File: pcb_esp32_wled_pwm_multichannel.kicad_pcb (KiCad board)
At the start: 4 copper layers, 164.6 x 48.3 mm, 94 parts, among them J101 WJ2EDGRC-5.08-4P, J102 WJ2EDGRC-5.08-4P, J103 WJ2EDGRC-5.08-4P, J104 WJ2EDGRC-5.08-4P, J105 Conn_01x05_Male, J106 Conn_01x03_Female, J107 Conn_01x03_Female, J108 Conn_01x02_Female, J109 USB_C_Receptacle_USB2.0, Q101 IRLR8743TRPBF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

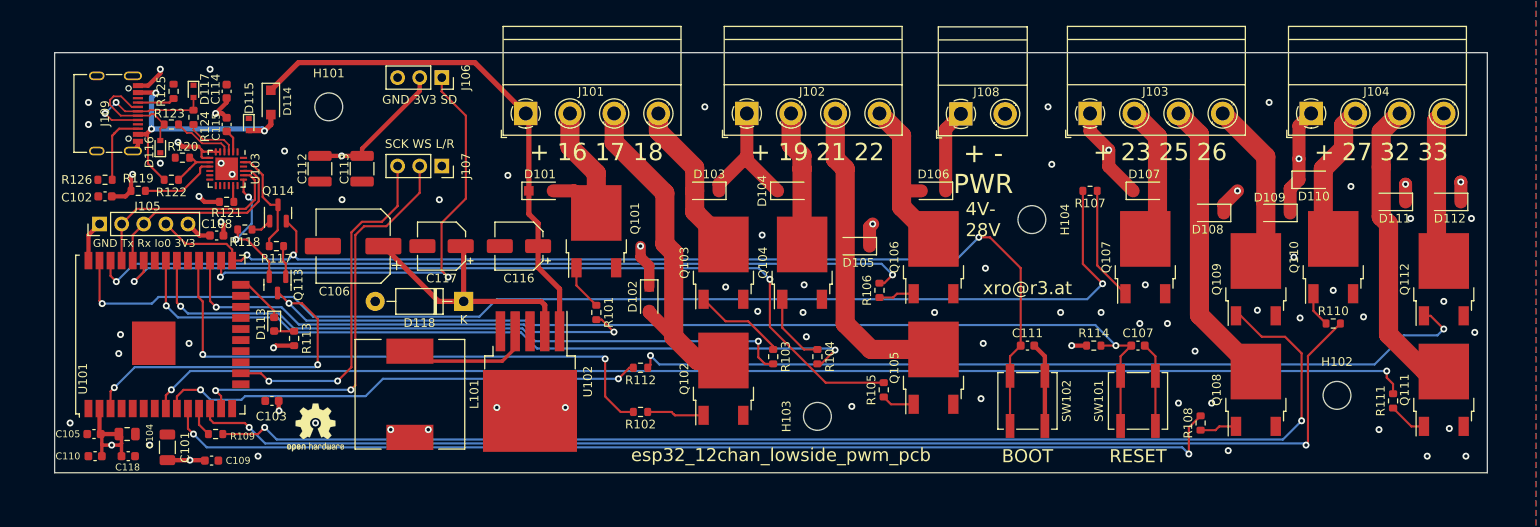
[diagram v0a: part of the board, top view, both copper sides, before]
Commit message: change footprint of polarized C to larger version that actually exists. Update BOM
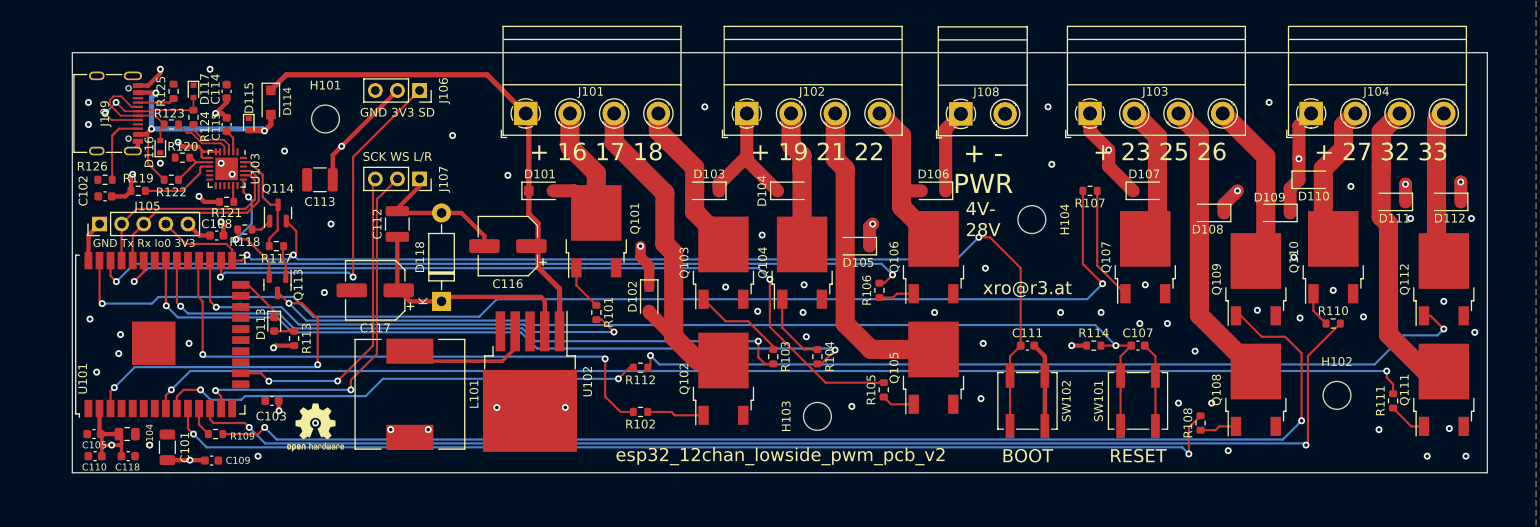
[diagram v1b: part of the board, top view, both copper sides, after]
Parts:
- removed C106: 470uF/20V, Capacitor_SMD:CP_Elec_8x11.9
- C116, C117: footprint Capacitor_SMD:CP_Elec_5x5.4 -> Capacitor_SMD:CP_Elec_6.3x7.7
- moved C112 10.9 mm to (47.0, 57.1), turned to 90 degrees
- moved C117 9.16 mm to (44.5, 64.8)
- moved C113 5.00 mm to (38.1, 52.1), turned to 180 degrees
- moved J106 2.95 mm to (49.5, 41.8)
- moved J107 2.95 mm to (49.5, 52.0)
- moved D118 2.54 mm to (52.1, 66.0), turned to 90 degrees
- moved H101 1.45 mm to (38.7, 45.1)
- moved C116 1.27 mm to (59.7, 59.7)
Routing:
- net GND: track 36.2 -> 53.3 mm, vias 60 -> 62
- net /I2S_SD: track 54.1 -> 42.2 mm
- net +3V3: track 88.2 -> 81.5 mm
- net /I2S_SM: track 48.4 -> 44.4 mm
- net /I2S_SCK: track 40.4 -> 36.5 mm
- net VDD: track 123.5 -> 122.3 mm
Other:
- board size 164.6 x 48.3 mm -> 162.6 x 48.3 mm
- board text added: "esp32_12chan_lowside_pwm_pcb_v2"
- board text removed: "esp32_12chan_lowside_pwm_pcb"

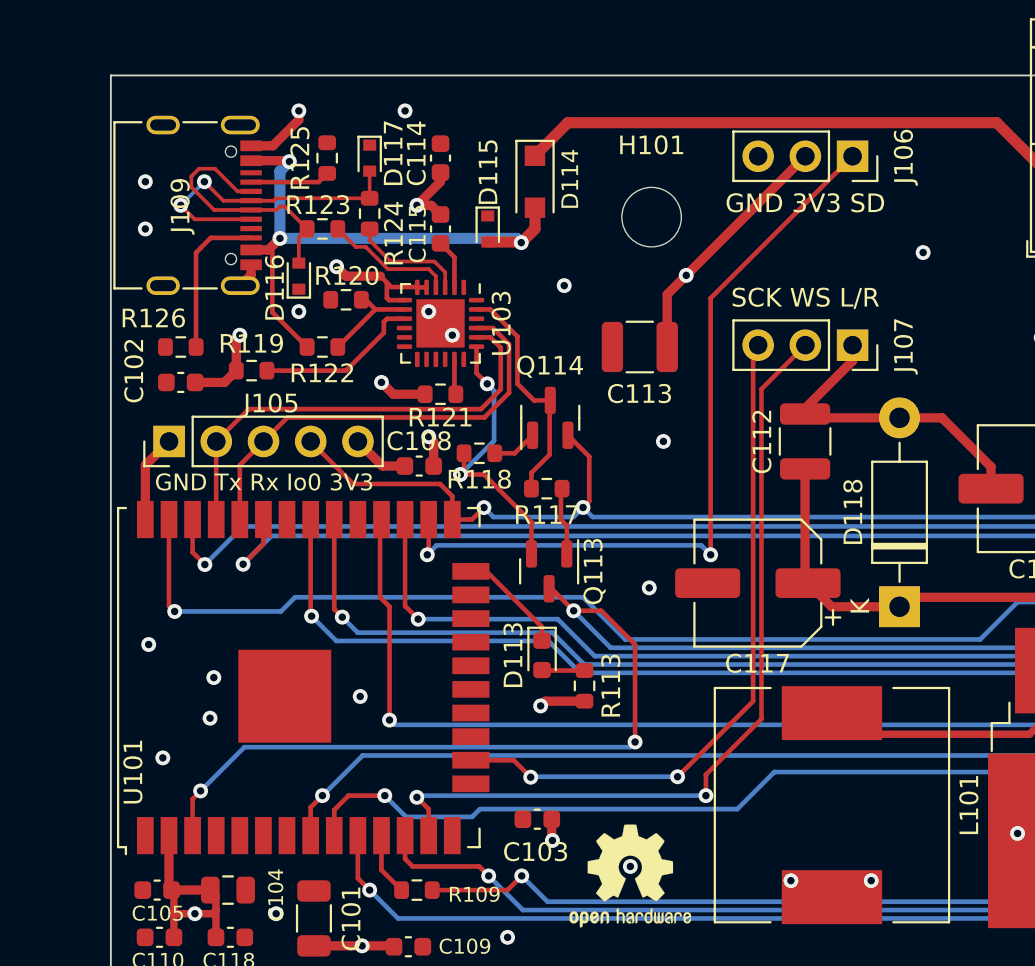
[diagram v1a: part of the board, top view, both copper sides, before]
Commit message: fix I2S microphone pin header. V3
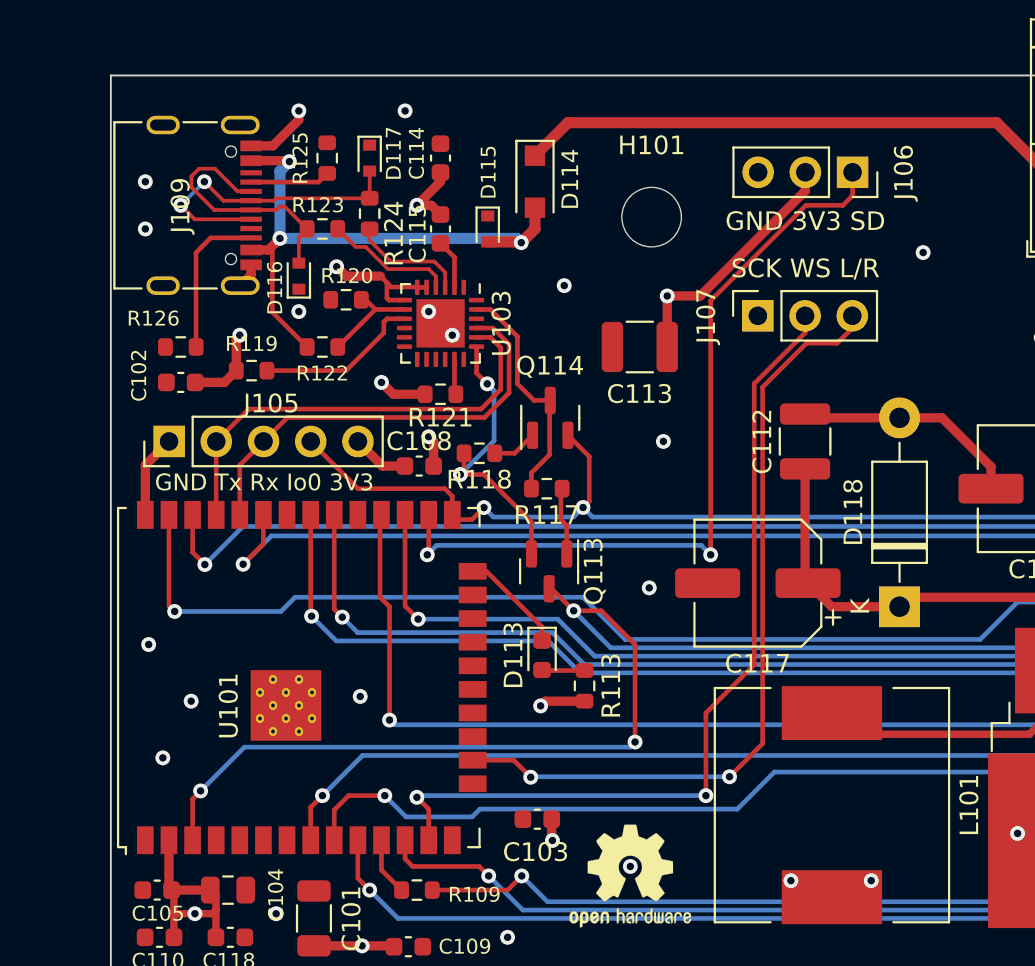
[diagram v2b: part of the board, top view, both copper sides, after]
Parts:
- C117: value 330µF/16V -> 330µF/6.3V
- moved J107 5.33 mm to (44.5, 50.4), turned to 90 degrees
- moved J106 0.86 mm to (49.5, 42.7)
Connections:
- net /RXD renamed /RXcp21
- net /RXD0 renamed /RXDesp
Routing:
- net /I2S_SCK: track 36.5 -> 42.8 mm
- net GND: track 53.3 -> 48.8 mm, vias 62 -> 61
- net /I2S_SM: track 44.4 -> 45.9 mm

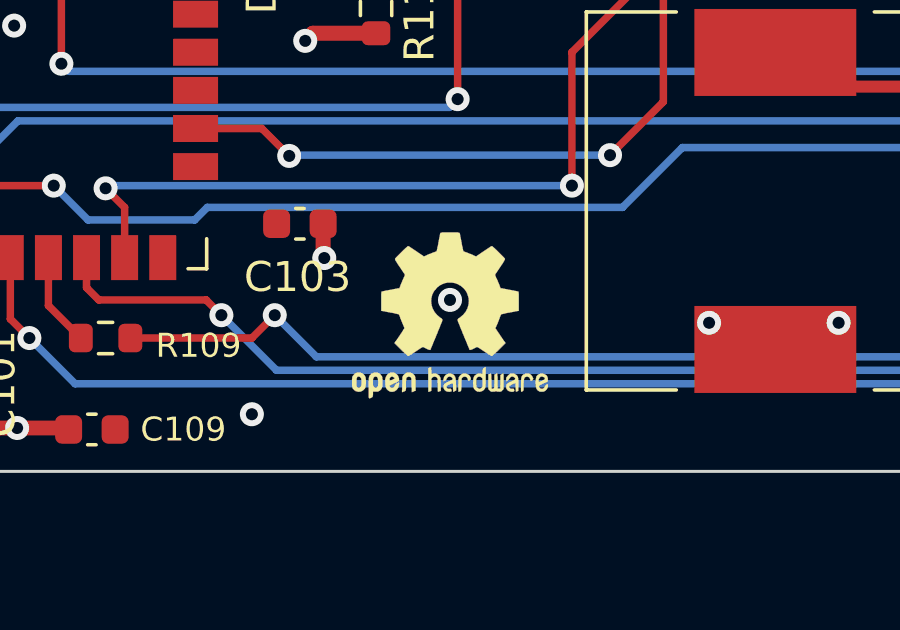
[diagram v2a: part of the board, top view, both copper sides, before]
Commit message: update future v3: reduce capacity of C111 debouncing BOOT0/IO0, so we are less likely to enter bootloader-mode on power-up
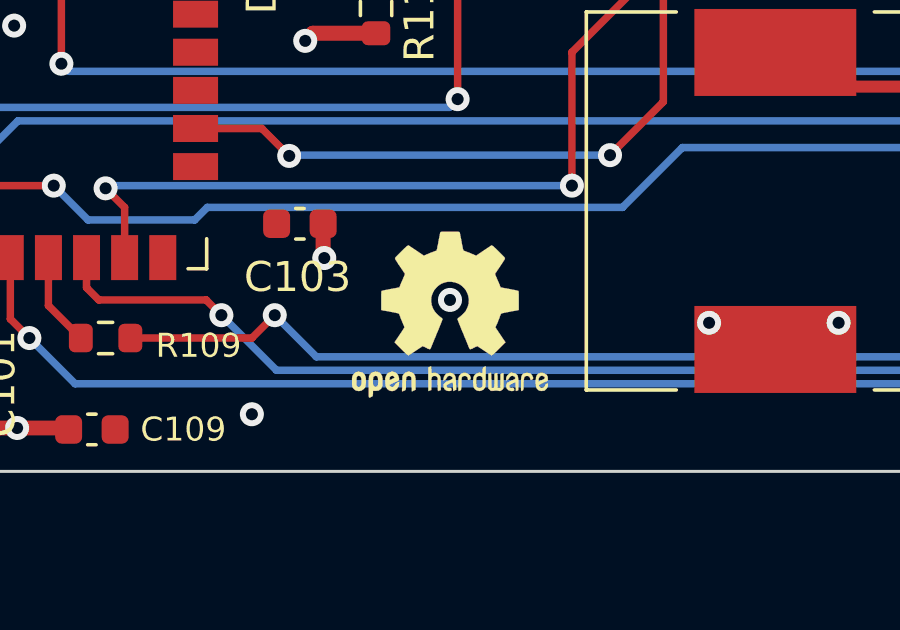
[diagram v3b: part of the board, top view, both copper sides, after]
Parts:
- removed REF**: OSHW-Logo2_7.3x6mm_SilkScreen, Symbol:OSHW-Logo2_7.3x6mm_SilkScreen
- added SYM101: Logo_Open_Hardware_Small, Symbol:OSHW-Logo2_7.3x6mm_SilkScreen, F.Cu at (37.6, 80.5)
- C111: value 100nF/50V -> 1nF/50V

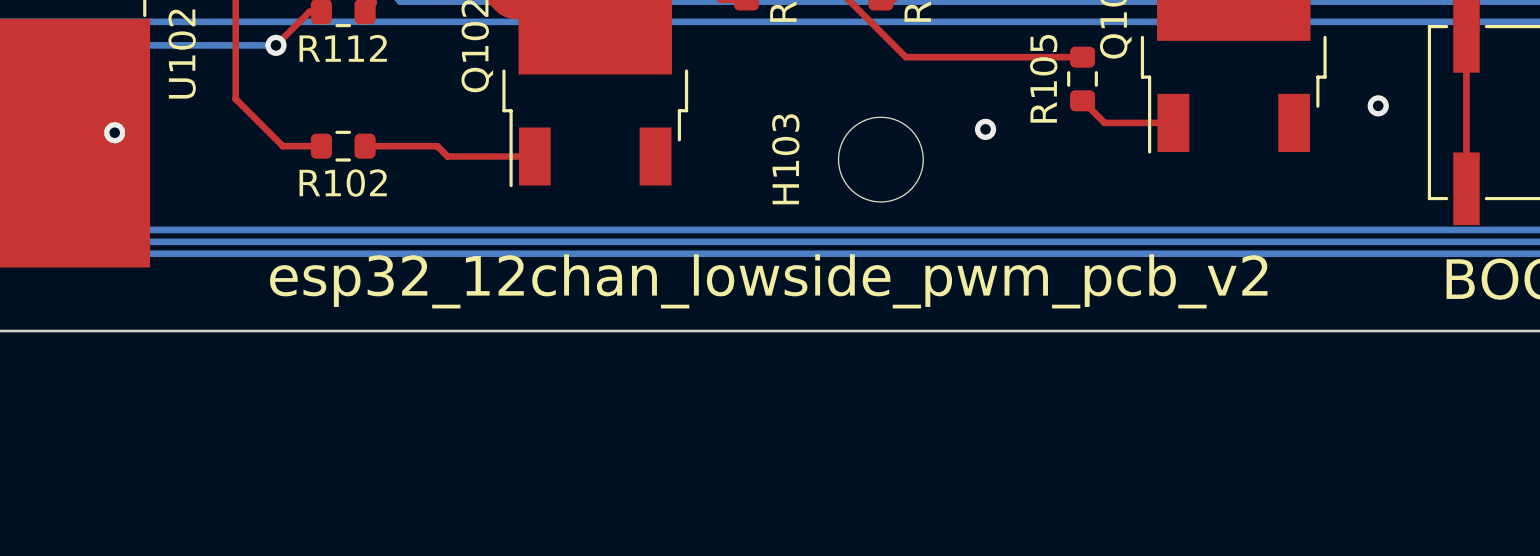
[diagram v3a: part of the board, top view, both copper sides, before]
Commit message: label as v3 on silkscreen
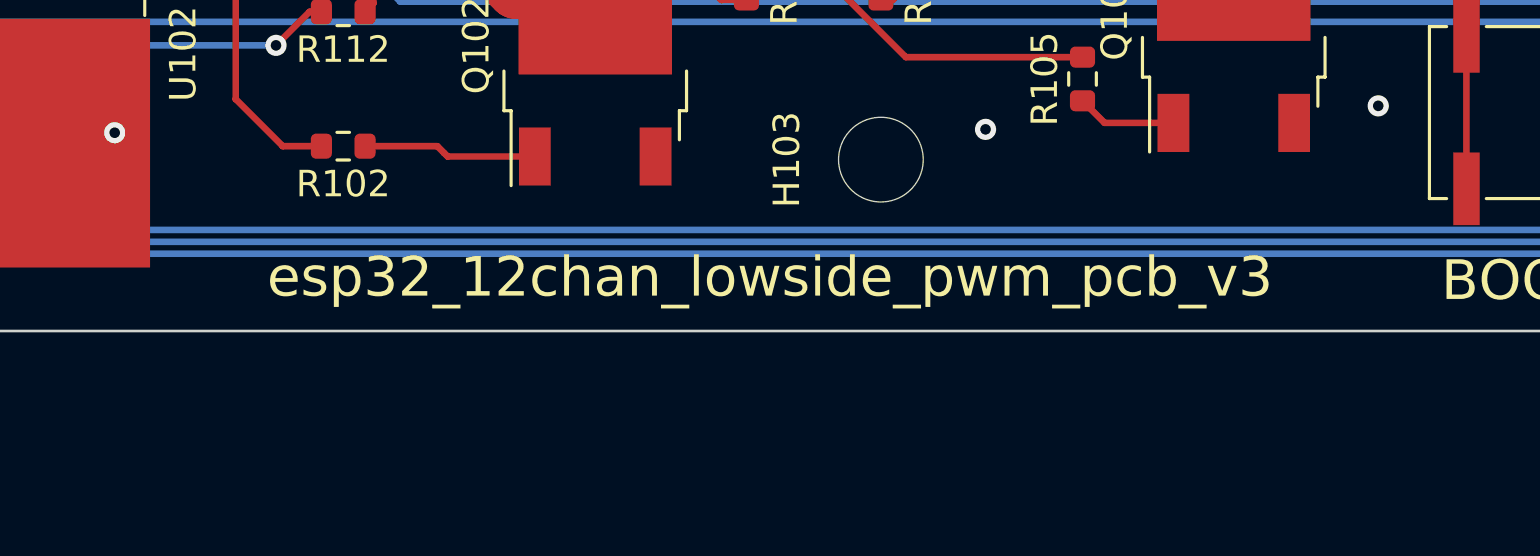
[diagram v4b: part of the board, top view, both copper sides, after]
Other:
- board text added: "esp32_12chan_lowside_pwm_pcb_v3"
- board text removed: "esp32_12chan_lowside_pwm_pcb_v2"
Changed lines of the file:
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@@
     (effects (font (size 1 1) (thickness 0.2)))
   )
-  (gr_text "esp32_12chan_lowside_pwm_pcb_v2" (at 91.059 83.693) (layer "F.SilkS")
+  (gr_text "esp32_12chan_lowside_pwm_pcb_v3" (at 91.059 83.693) (layer "F.SilkS")
     (effects (font (size 1.5 1.5) (thickness 0.3)))
   )

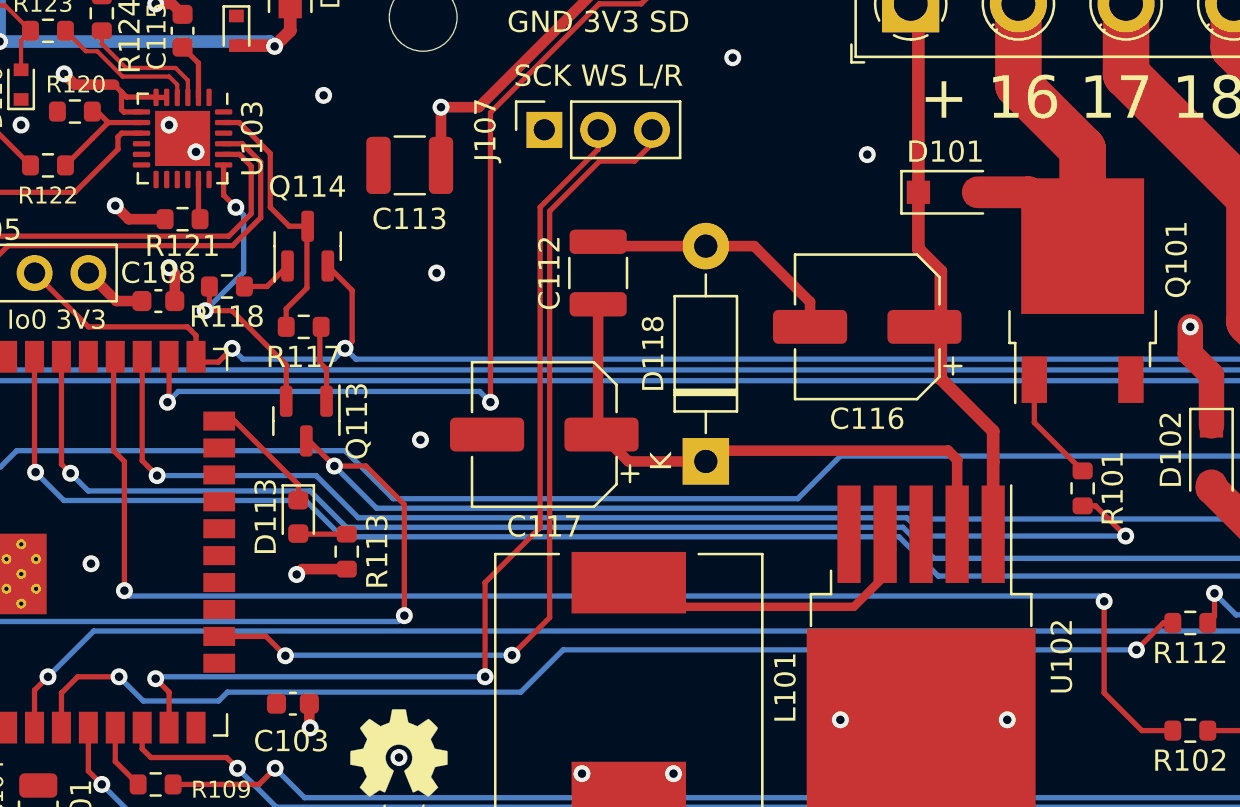
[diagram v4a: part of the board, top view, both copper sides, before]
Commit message: several fixes, thanks to mickdermack for reviewing
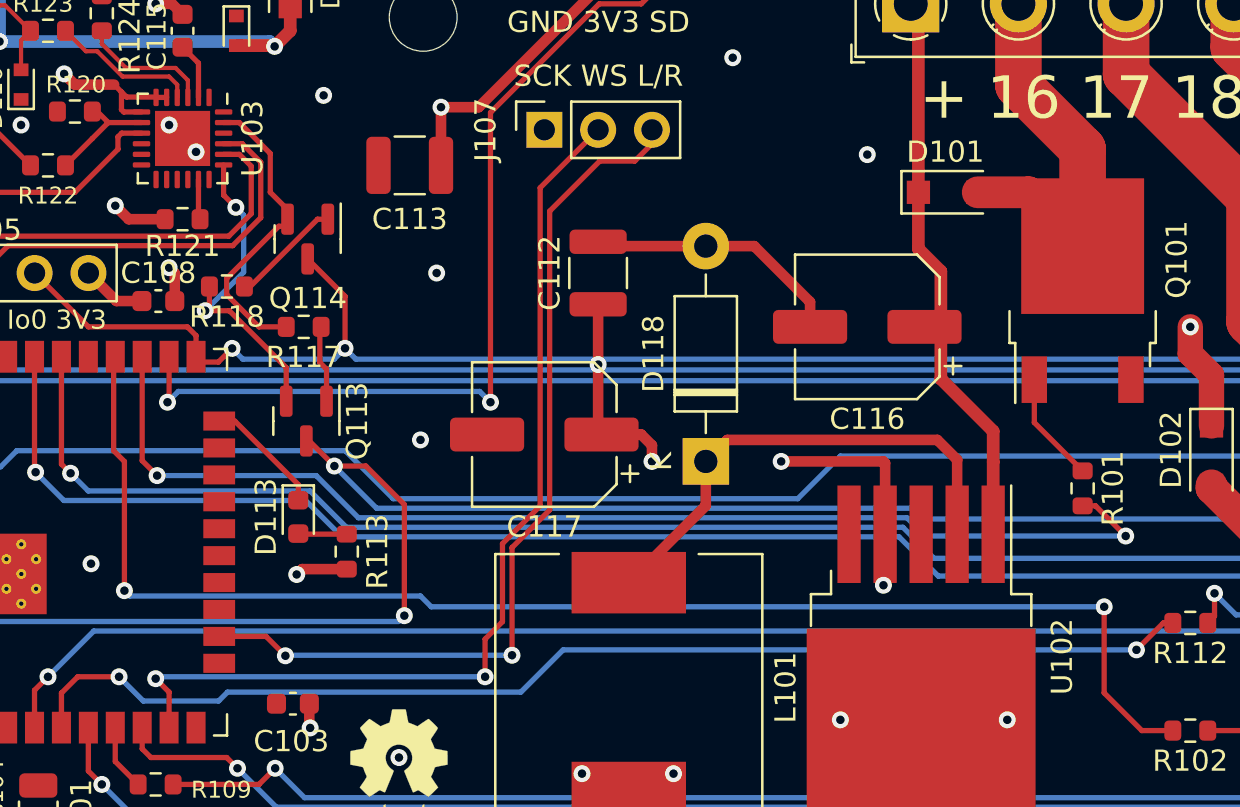
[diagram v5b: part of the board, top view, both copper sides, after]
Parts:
- moved Q114 0.33 mm to (33.3, 55.5), turned to -90 degrees
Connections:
- D118 pad 1: +3V3 -> Net-(D118-K)
- L101 pad 1: Net-(U102-FB) -> Net-(D118-K)
- Q114 pad 2: /IO0 -> /DTR
- Q114 pad 3: /DTR -> /IO0
- U102 pad 2: +3V3 -> Net-(D118-K)
- U102 pad 4: Net-(U102-FB) -> +3V3
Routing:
- net Net-(D118-K): track 0.00 -> 23.4 mm
- net Net-(U102-FB): track 15.1 -> 0.00 mm
- net +3V3: track 81.7 -> 74.6 mm, vias 11 -> 15
- net Net-(Q114-B): track 2.44 -> 5.25 mm
- net /DTR: track 12.6 -> 14.7 mm
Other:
- board text added: "+ - 4-28V"
- board text removed: "+ - 5-30V"
